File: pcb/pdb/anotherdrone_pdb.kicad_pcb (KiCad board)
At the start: 2 copper layers, 107.2 x 101 mm, 28 parts, among them J1 BATT, J10 STAT, J11 MCU, J12 5v, J3 3v, J6 ESC A, J7 ESC B, J8 ESC C, J9 ESC D, P1 ESC Power A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

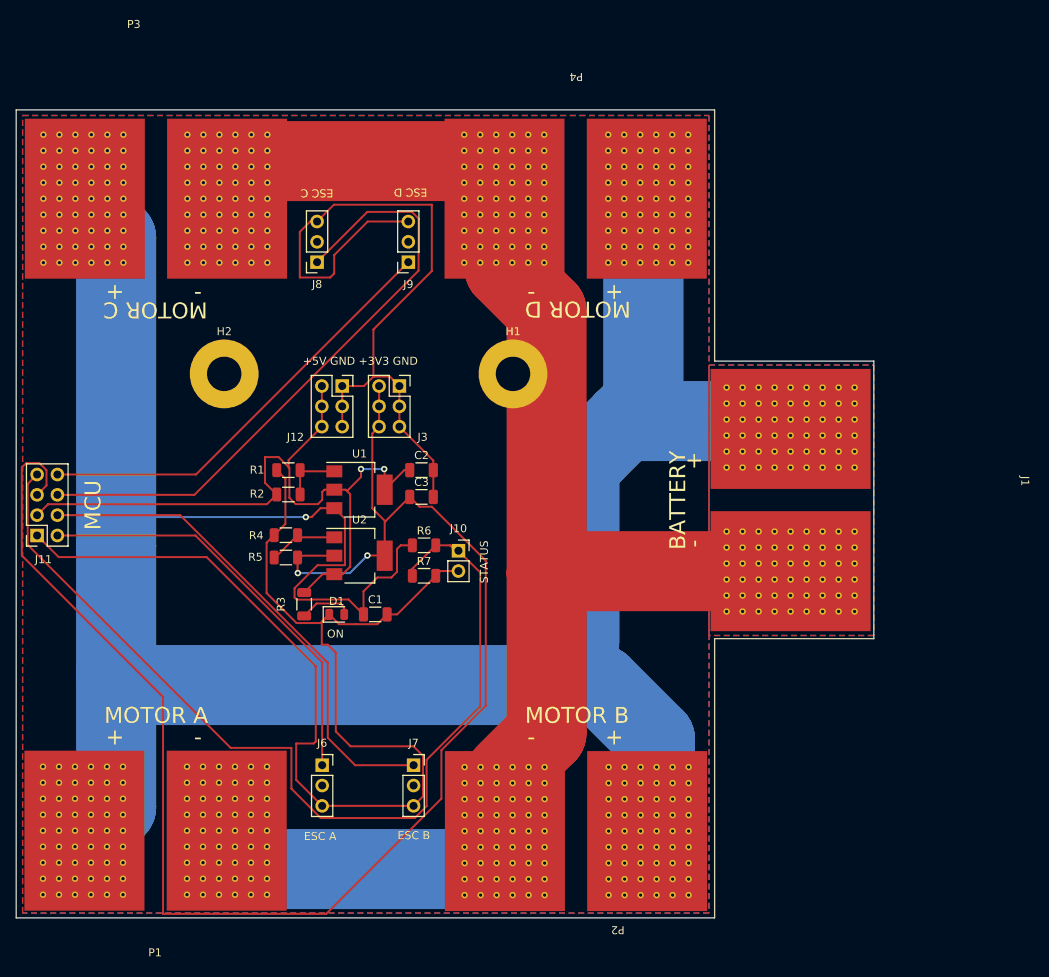
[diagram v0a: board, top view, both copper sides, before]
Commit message: now using 15v and ground planes
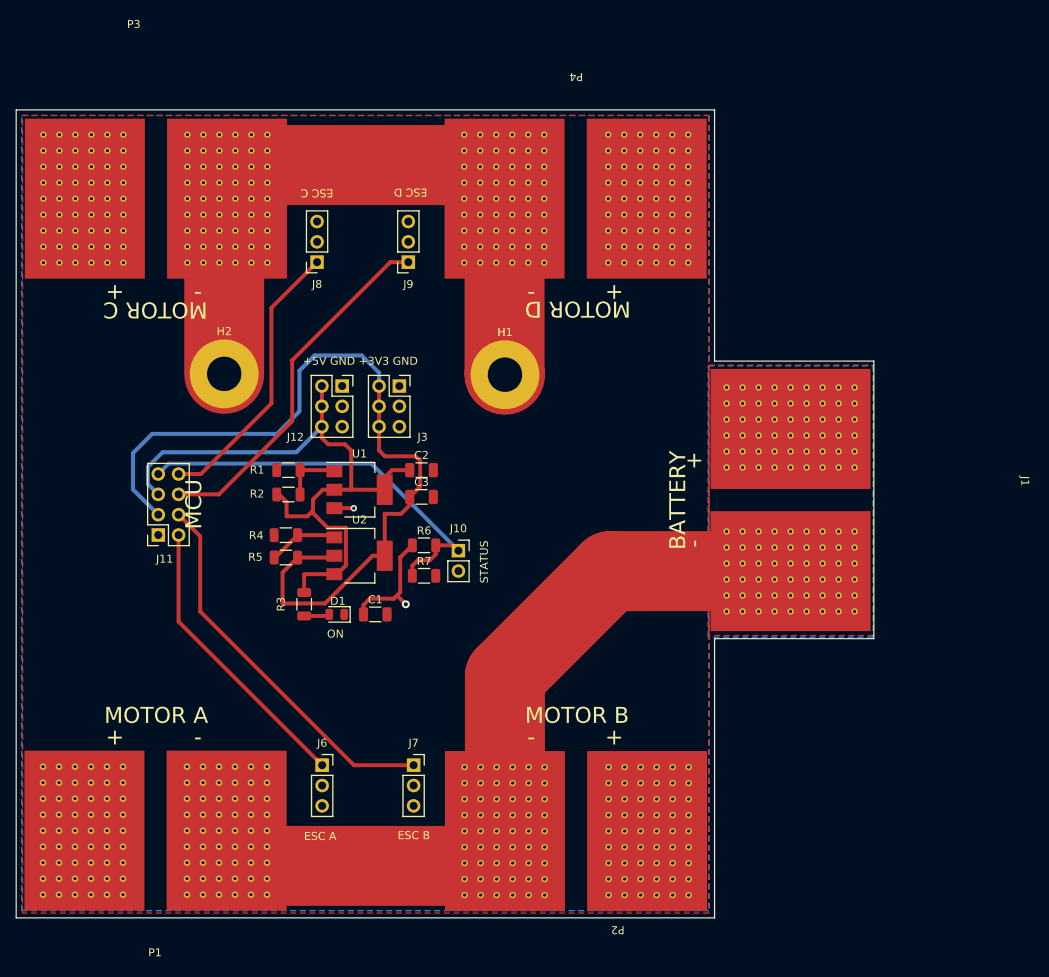
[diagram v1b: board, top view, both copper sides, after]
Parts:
- moved J11 15.2 mm to (85.6, 91.2)
- moved H1 1.00 mm to (128.9, 71.2)
- turned D1 to 180 degrees
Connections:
- J11 pad 3: +5V -> +3V3
- J11 pad 5: +3V3 -> +5V
- J11 pad 6: Signal C -> Signal D
- J11 pad 8: Signal D -> Signal C
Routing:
- net +15V: track 306.7 -> 16.9 mm, vias 1 -> 2
- net GND: track 439.8 -> 181.2 mm
- net +3V3: track 201.0 -> 106.1 mm, vias 2 -> 0
- net STAT: track 120.9 -> 51.6 mm
- net Signal C: track 78.9 -> 35.3 mm
- net Signal A: track 52.5 -> 36.2 mm
- net Signal B: track 63.0 -> 47.9 mm
- net +5V: track 94.3 -> 84.2 mm, vias 2 -> 0
- net Signal D: track 54.9 -> 45.2 mm
- net Net-(D1-Pad2): track 6.72 -> 3.21 mm
- added copper zone on B.Cu, net +15V
- removed copper zone on B.Cu, net GND

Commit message: added logo
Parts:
- added G***: LOGO, brw:brw_logo, F.Cu at (77.2, 103.5)
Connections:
- H1 pad 1: GND -> (no net)
- H2 pad 1: GND -> (no net)
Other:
- board text added: "AnotherDrone PDB - V 0.1"
